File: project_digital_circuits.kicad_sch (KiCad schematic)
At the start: 7 parts, among them M1 Motor_DC, M2 Motor_DC, U1 TB6612FNG

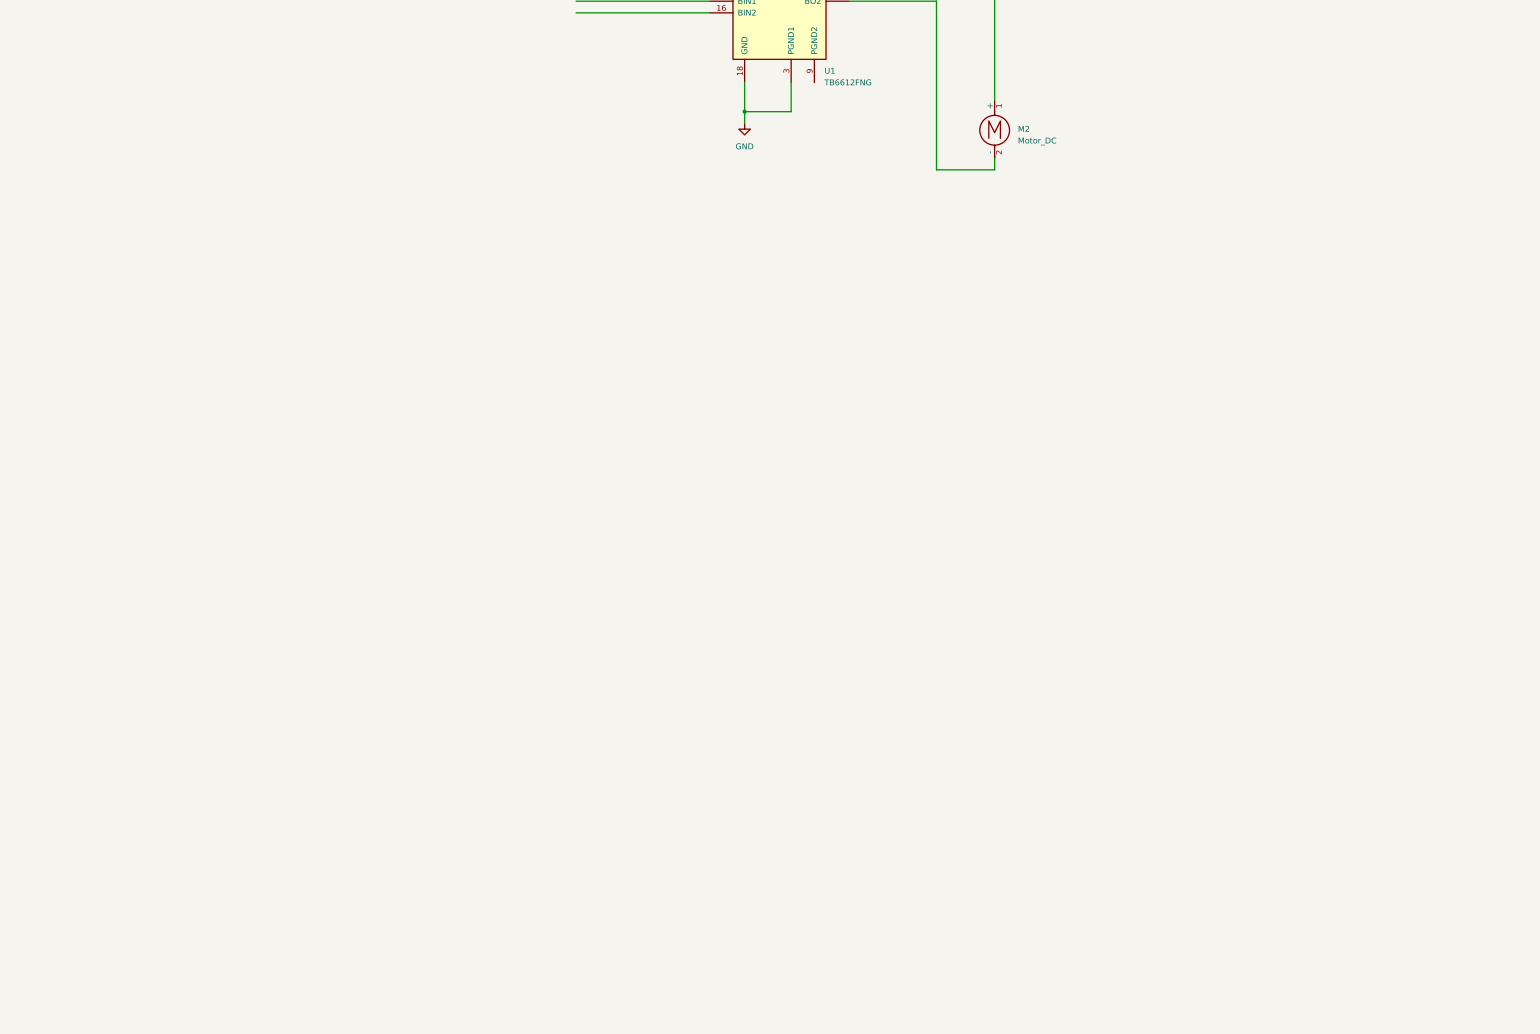
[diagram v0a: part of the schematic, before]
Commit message: ESP-32 added with peripherals with power menagement
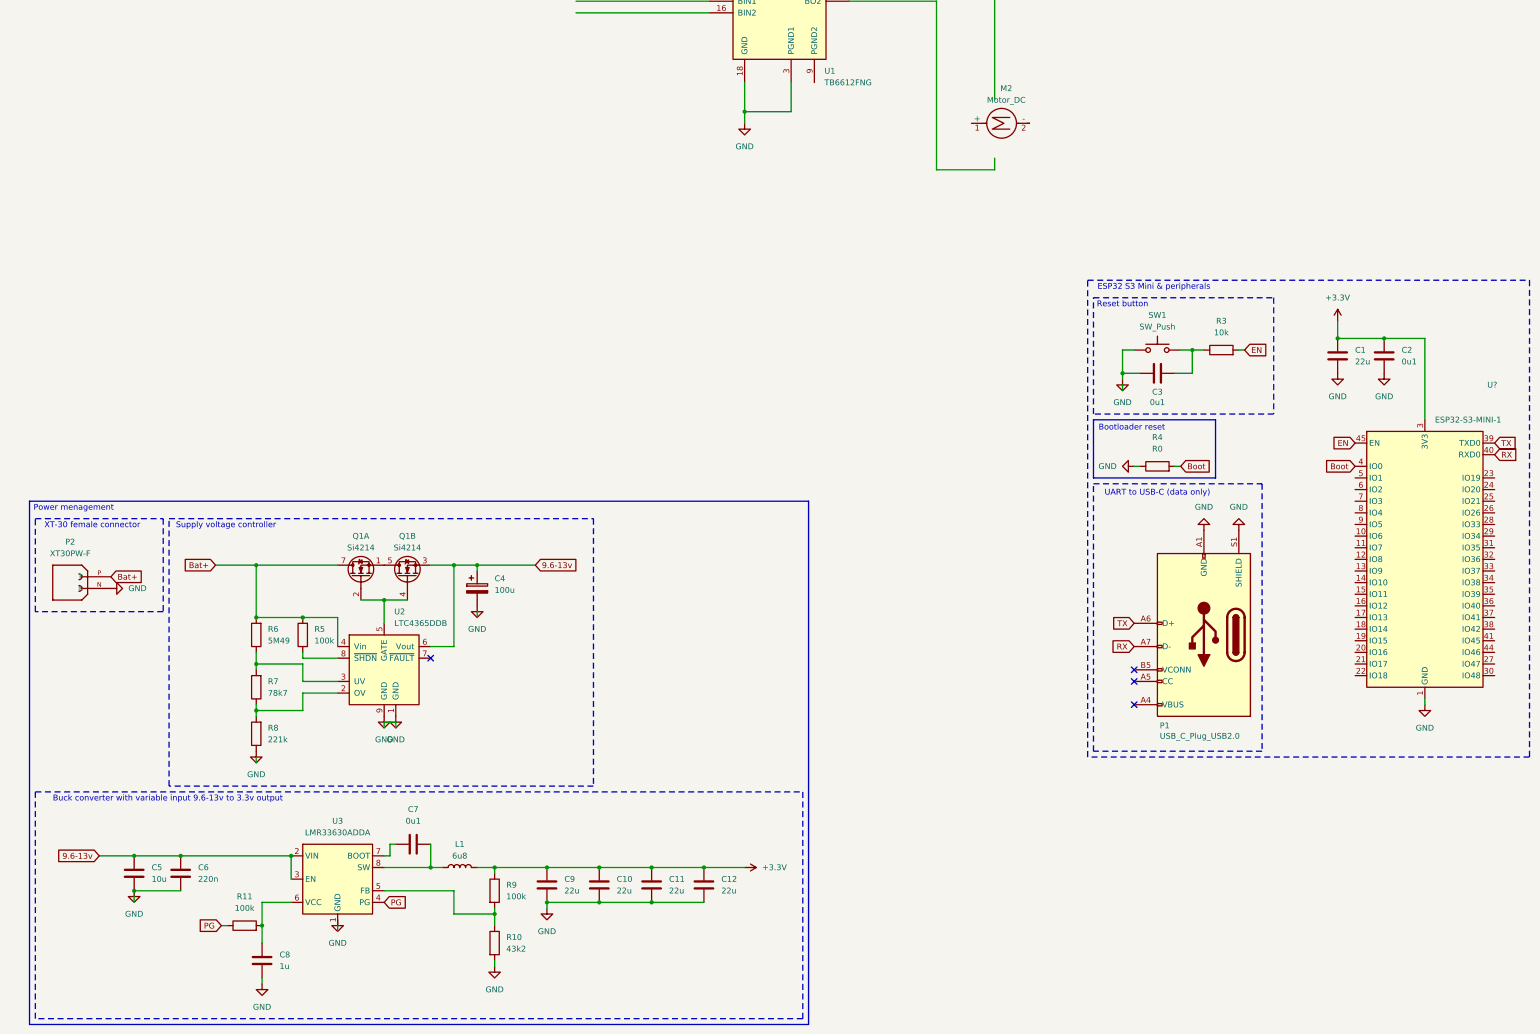
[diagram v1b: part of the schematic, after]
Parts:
- added C1, C10, C11, C12, C9: 22u, symbol Device:C
- added C2, C3, C7: 0u1, symbol Device:C
- added C4: 100u, symbol Device:C_Polarized
- added C5: 10u, symbol Device:C
- added C6: 220n, symbol Device:C
- added C8: 1u, symbol Device:C
- added L1: 6u8, symbol Device:L
- added P1: USB_C_Plug_USB2.0, symbol Connector:USB_C_Plug_USB2.0
- added P2: XT30PW-F, XT30PW-F:AMASS_XT30PW-F, symbol XT30PW-F:XT30PW-F
- added Q1: Si4214, Package_SO:SOIC-8_3.9x4.9mm_P1.27mm, symbol Transistor_FET:STS2DNE60
- added R10: 43k2, symbol Device:R
- added R11, R5, R9: 100k, symbol Device:R
- added R3: 10k, symbol Device:R
- added R4: R0, symbol Device:R
- added R6: 5M49, symbol Device:R
- added R7: 78k7, symbol Device:R
- added R8: 221k, symbol Device:R
- added SW1: SW_Push, symbol Switch:SW_Push
- added U2: LTC4365DDB, Package_DFN_QFN:DFN-8-1EP_2x3mm_P0.5mm_EP0.61x2.2mm, symbol Power_Management:LTC4365DDB
- added U3: LMR33630ADDA, Package_SO:Texas_HSOP-8-1EP_3.9x4.9mm_P1.27mm_ThermalVias, symbol Regulator_Switching:LMR33630ADDA
- added U?: ESP32-S3-MINI-1, RF_Module:ESP32-S2-MINI-1, symbol RF_Module:ESP32-S3-MINI-1
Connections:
- net GND: now also C1.2, C10.2, C11.2, C12.2, C2.2, C3.2, C4.2, C5.2, C6.2, C8.2, C9.2, P1.A1 (GND), P1.A12 (GND), P1.B1 (GND), P1.B12 (GND), P1.S1 (SHIELD), P2.N, R10.2, R4.1, R8.1, SW1.1, U2.1 (GND), U2.9 (GND), U?.1 (GND), U?.2 (GND), U?.42 (GND), U?.43 (GND), U?.46 (GND), U?.47 (GND), U?.48 (GND), U?.49 (GND), U?.50 (GND), U?.51 (GND), U?.52 (GND), U?.53 (GND), U?.54 (GND), U?.55 (GND), U?.56 (GND), U?.57 (GND), U?.58 (GND), U?.59 (GND), U?.60 (GND), U?.61 (GND), U?.62 (GND), U?.63 (GND), U?.64 (GND), U?.65 (GND)
- net at U1.11 (BO1), U1.12 (BO1): no longer M2.1 (+)
- net at U1.7 (BO2), U1.8 (BO2): no longer M2.2 (-)
- new net: R7.1, R8.2, U2.2 (OV)
- new net: R6.1, R7.2, U2.3 (UV)
- new net: Q1.2 (G1), Q1.4 (G2), U2.5 (GATE)
- new net: R5.1, U2.8 (~{SHDN})
- new net: C7.1, L1.1, U3.8 (SW)
- new net: C7.2, U3.7 (BOOT)
- new net: C8.1, R11.2, U3.6 (VCC)
- new net: R10.1, R9.2, U3.5 (FB)
- new net: C3.1, R3.1, SW1.2
- new net: U3.1 (GND), U3.9 (GND)
- new net: Q1.1 (S1), Q1.5 (D2), Q1.6 (D2)
- new net: P1.A4 (VBUS), P1.A9 (VBUS), P1.B4 (VBUS), P1.B9 (VBUS)
- new net +3.3V: C1.1, C10.1, C11.1, C12.1, C2.1, C9.1, L1.2, R9.1, U?.3 (3V3)
- new net 9.6-13v: C4.1, C5.1, C6.1, Q1.3 (S2), U2.6 (Vout), U3.2 (VIN), U3.3 (EN)
- new net Bat+: P2.P, Q1.7 (D1), Q1.8 (D1), R5.2, R6.2, U2.4 (Vin)
- new net Boot: R4.2, U?.4 (IO0)
- new net EN: R3.2, U?.45 (EN)
- new net PG: R11.1, U3.4 (PG)
- new net RX: P1.A7 (D-), U?.40 (RXD0)
- new net TX: P1.A6 (D+), U?.39 (TXD0)
- no-connect marks 0 -> 4
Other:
- note added: "Bootloader reset"
- note added: "Buck converter with variable input 9.6-13v to 3.3v output"
- note added: "ESP32 S3 Mini & peripherals"
- note added: "Power menagement"
- note added: "Reset button"
- note added: "Supply voltage controller"
- note added: "UART to USB-C (data only)"
- note added: "XT-30 female connector"
- moved on the sheet: M2

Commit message: Sensors connections
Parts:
- added C13: 10n, symbol Device:C
- added C14, C16: 0u1, symbol Device:C
- added C15: 2n2, symbol Device:C
- added J1: Grove - universal connector 4-pin, symbol Connector:Conn_01x04_Socket
- added Q2, Q3: Si4214, Package_TO_SOT_THT:TO-92_Inline, symbol Transistor_FET:BS108
- added R12, R13: 4k7, symbol Device:R
- added R14, R15, R16, R17: 10k, symbol Device:R
- added R18, R19: 47k, symbol Device:R
- added U4: MPU-6050, Sensor_Motion:InvenSense_QFN-24_4x4mm_P0.5mm, symbol Sensor_Motion:MPU-6050
- added U5: VL53L0CXV0DH1, Sensor_Distance:ST_VL53L1x, symbol Sensor_Distance:VL53L0CXV0DH1
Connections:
- net +3.3V: now also C13.1, C16.1, R12.1, R13.1, U4.13 (VDD), U4.8 (VLOGIC)
- net GND: now also C13.2, C14.2, C15.2, C16.2, J1.1 (Pin_1), U4.1 (CLKIN), U4.11 (FSYNC), U4.18 (GND), U5.12 (GND), U5.2 (AVSSVCSEL), U5.3 (GND), U5.4 (GND), U5.6 (GND)
- new net: Q3.3 (S), R17.1, U5.10 (SCL)
- new net: R19.1, U5.5 (XSHUT)
- new net: R18.1, U5.7 (GPIO1)
- new net: Q2.3 (S), R16.1, U5.9 (SDA)
- new net: R12.2, U4.24 (SDA)
- new net: C15.1, U4.20 (CPOUT)
- new net: R13.2, U4.23 (SCL)
- new net: C14.1, U4.10 (REGOUT)
- new net +5V: J1.2 (Pin_2)
- new net SCL: J1.4 (Pin_4), Q3.1 (D), R14.1, R15.1
- new net SDA: J1.3 (Pin_3), Q2.1 (D)
- new net VCC +3.3V: U5.1 (AVDDVCSEL), U5.11 (AVDD)
- new net VDD: Q2.2 (G), Q3.2 (G), R16.2, R17.2, R18.2, R19.2
- new net VIN: R14.2, R15.2
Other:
- note added: "Accelometer and Gyroscope"
- note added: "Connection to distance sensor"
- note added: "Usune jesli Pan powie ze nie potrzebne"
- moved on the sheet: C1, C2, C3, Enc2, P1, R3, R4, SW1, U?

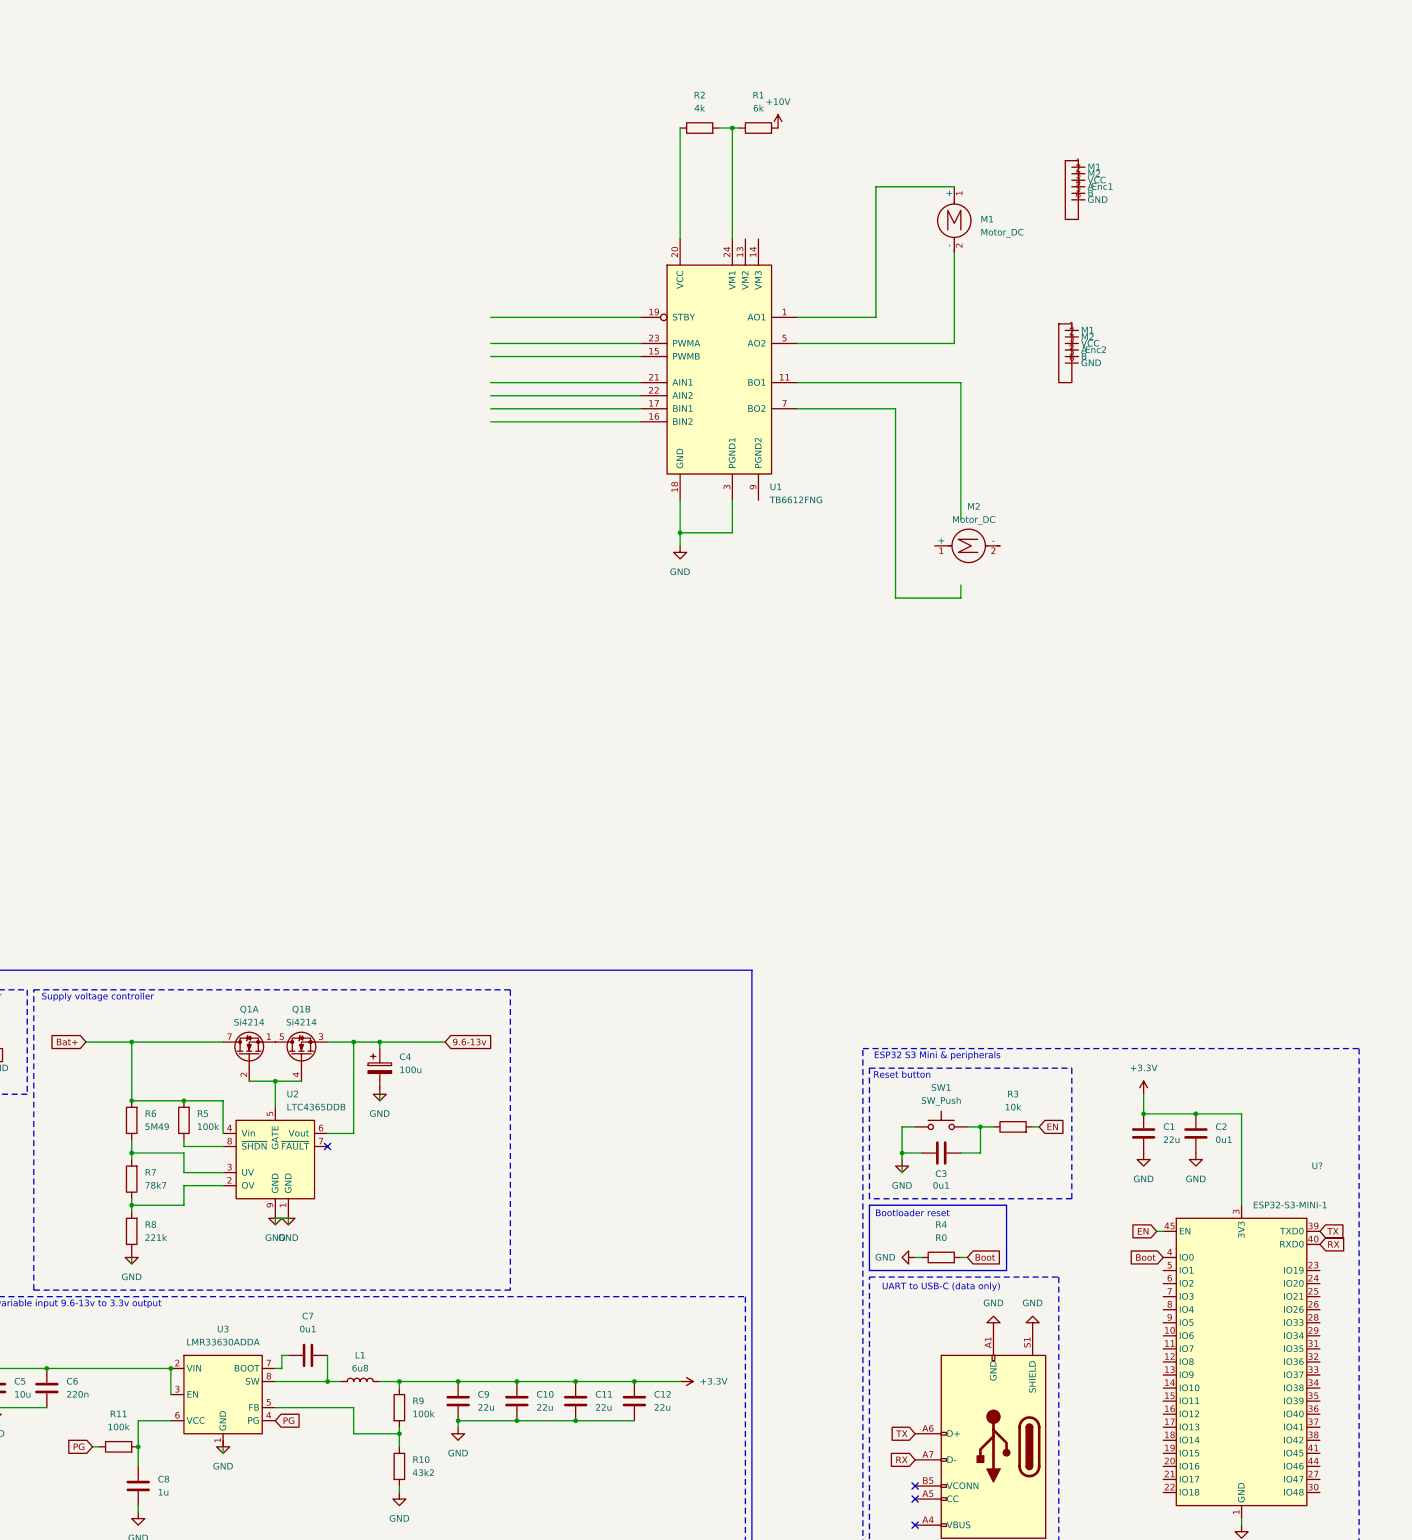
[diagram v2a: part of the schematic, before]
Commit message: Motor driver merged
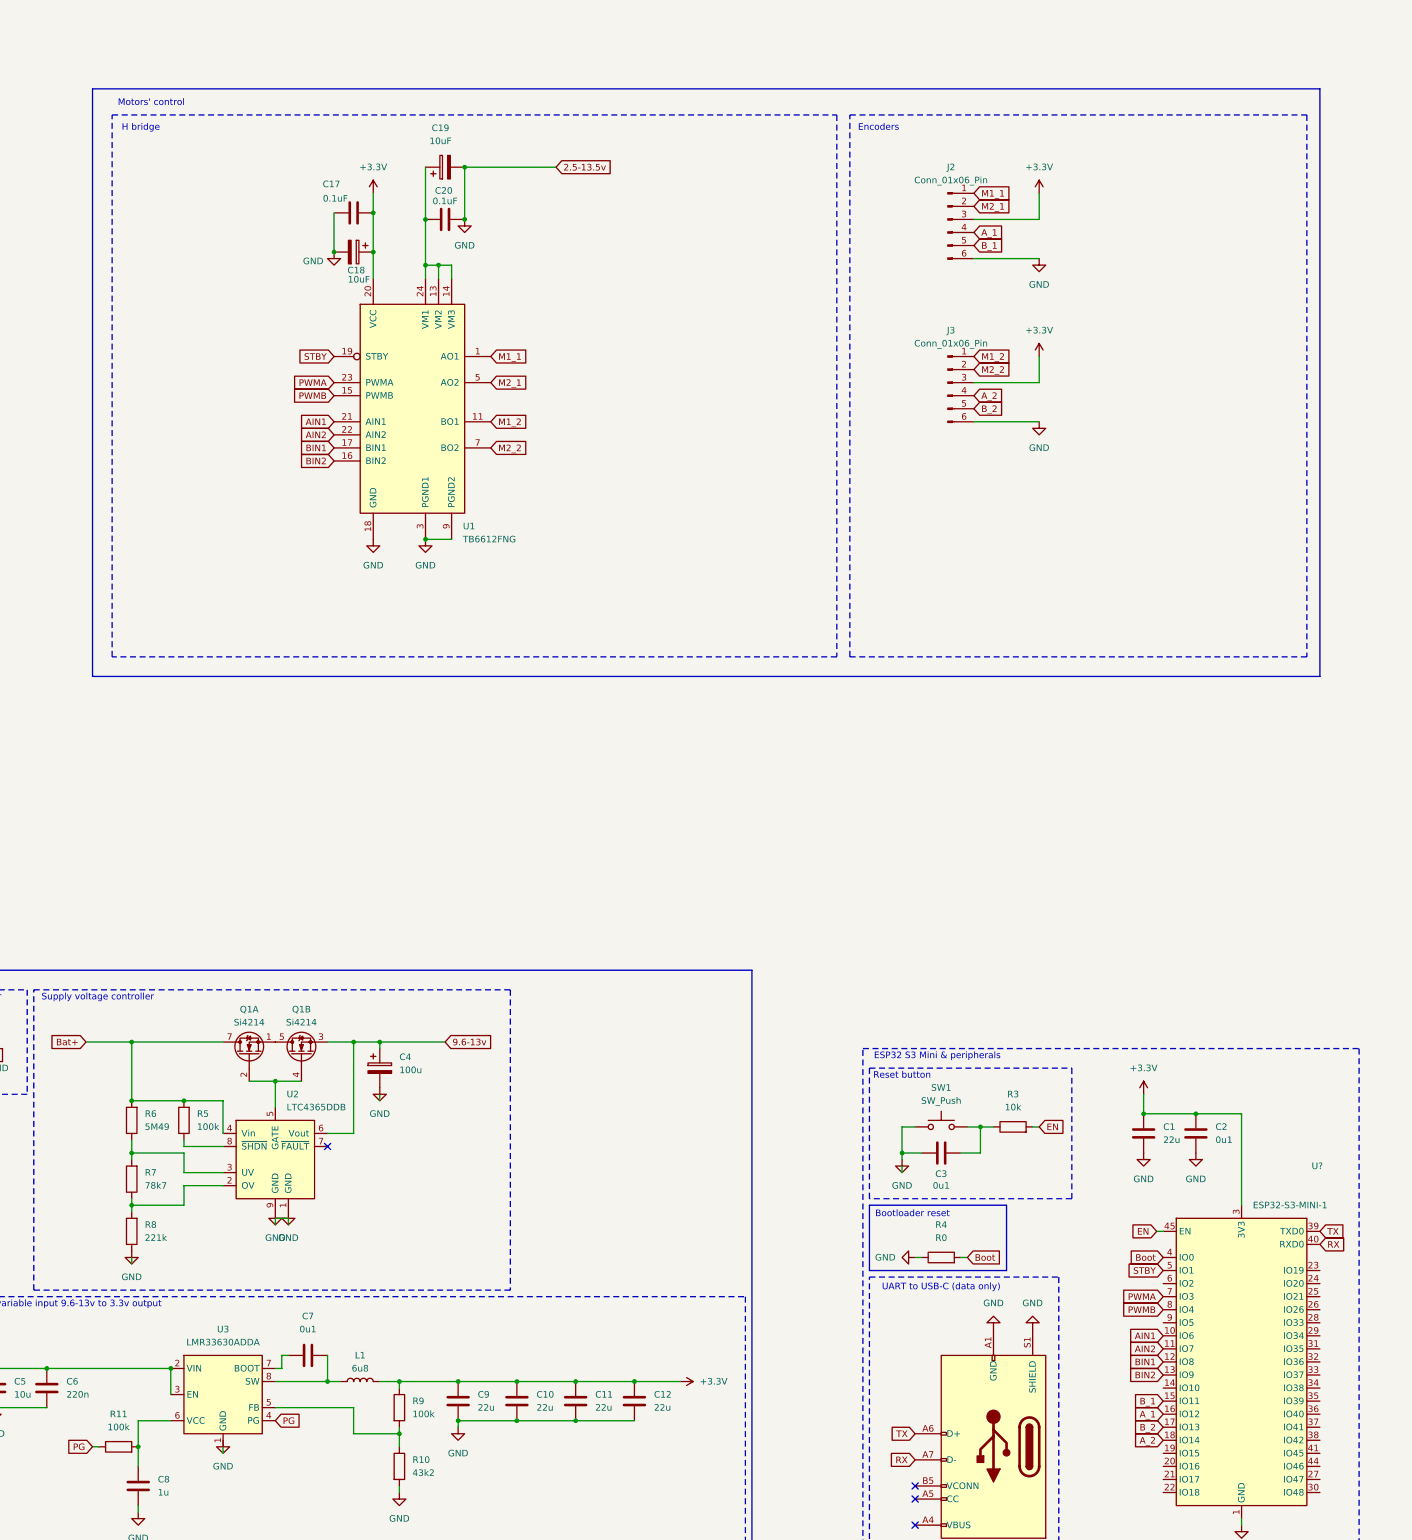
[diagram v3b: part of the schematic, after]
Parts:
- removed Enc1, Enc2: ~, symbol New_Library:Pololu_3081
- removed M1, M2: Motor_DC, symbol Motor:Motor_DC
- removed R1: 6k, symbol Device:R
- removed R2: 4k, symbol Device:R
- added C17, C20: 0.1uF, symbol Device:C
- added C18, C19: 10uF, symbol Device:C_Polarized
- added J2, J3: Conn_01x06_Pin, symbol Connector:Conn_01x06_Pin
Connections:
- net +3.3V: now also U1.20 (VCC), C17.2, C18.1, J2.3 (Pin_3), J3.3 (Pin_3)
- net GND: now also U1.10 (PGND2), U1.9 (PGND2), C17.1, C18.2, C19.2, C20.2, J2.6 (Pin_6), J3.6 (Pin_6)
- net at U1.24 (VM1): now also U1.13 (VM2), U1.14 (VM3), C19.1, C20.1
- net M1_1: now reaches U1.1 (AO1), U1.2 (AO1)
- net M1_1: now also J2.1 (Pin_1)
- net M1_2: now reaches U1.11 (BO1), U1.12 (BO1)
- net M1_2: now also J3.1 (Pin_1)
- net PWMB: now reaches U1.15 (PWMB)
- net PWMB: now also U?.8 (IO4)
- net BIN2: now reaches U1.16 (BIN2)
- net BIN2: now also U?.13 (IO9)
- net BIN1: now reaches U1.17 (BIN1)
- net BIN1: now also U?.12 (IO8)
- net STBY: now reaches U1.19 (STBY)
- net STBY: now also U?.5 (IO1)
- net AIN1: now reaches U1.21 (AIN1)
- net AIN1: now also U?.10 (IO6)
- net AIN2: now reaches U1.22 (AIN2)
- net AIN2: now also U?.11 (IO7)
- net PWMA: now reaches U1.23 (PWMA)
- net PWMA: now also U?.7 (IO3)
- net M2_1: now reaches U1.5 (AO2), U1.6 (AO2)
- net M2_1: now also J2.2 (Pin_2)
- net M2_2: now reaches U1.7 (BO2), U1.8 (BO2)
- net M2_2: now also J3.2 (Pin_2)
- net B_1: now reaches U?.15 (IO11)
- net B_1: now also J2.5 (Pin_5)
- net A_1: now reaches U?.16 (IO12)
- net A_1: now also J2.4 (Pin_4)
- net B_2: now reaches U?.17 (IO13)
- net B_2: now also J3.5 (Pin_5)
- net A_2: now reaches U?.18 (IO14)
- net A_2: now also J3.4 (Pin_4)
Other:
- note added: "Encoders"
- note added: "H bridge"
- note added: "Motors' control"
